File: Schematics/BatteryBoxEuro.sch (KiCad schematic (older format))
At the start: 16 parts, among them K1 JD2912-1Z-12VDC_40A, P1 Conn_WallPlug, U1 Terminal16, U2 F_Distributor, U3 NAC3MPA-1-WOT, U4 DPlusSimulator, U5 Pulser, U6 230V_KfzCharger, X1 X3, X2 12VKfz_Plug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

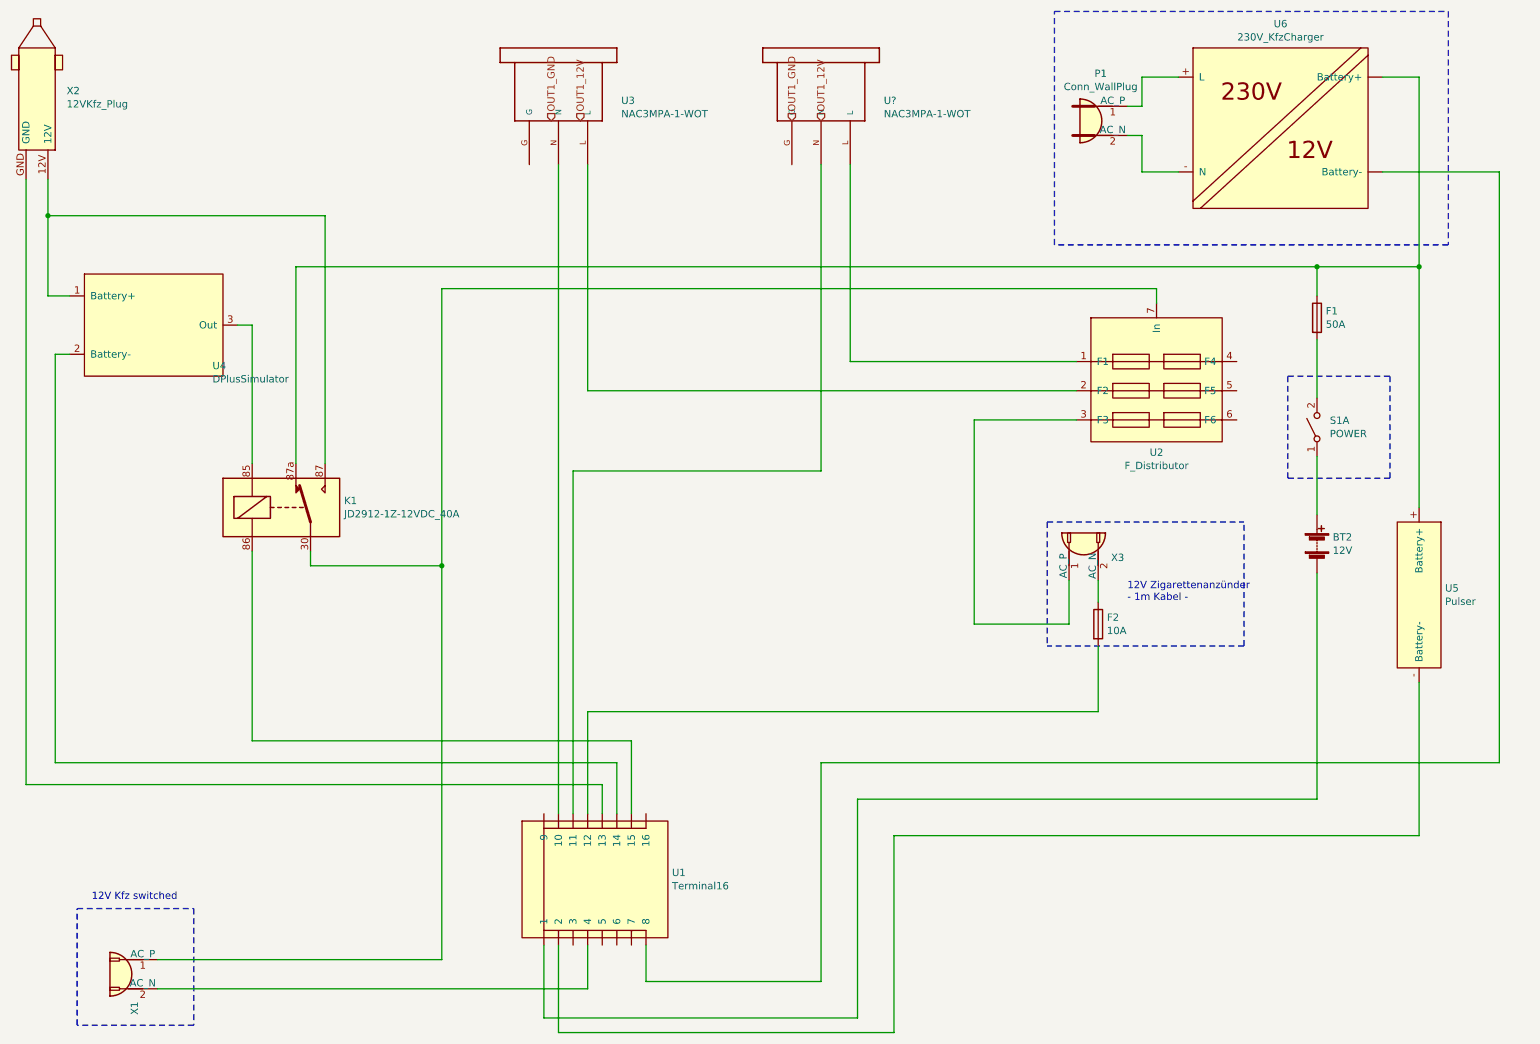
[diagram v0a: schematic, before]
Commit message: rearrange symbols
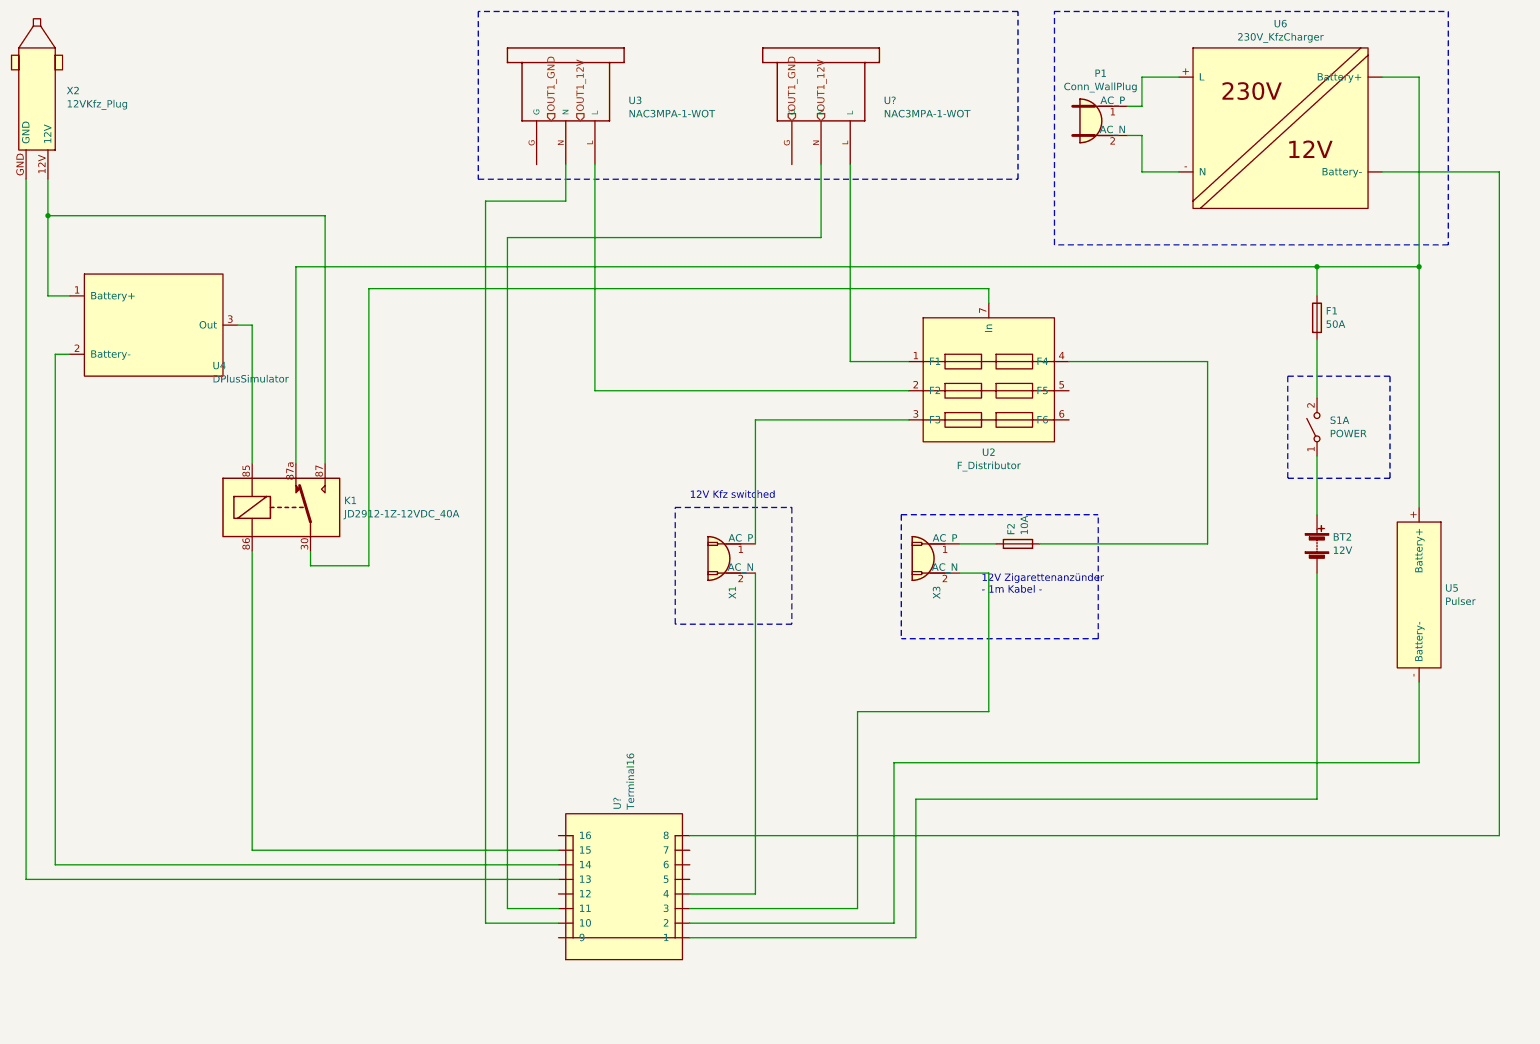
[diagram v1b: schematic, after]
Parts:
- removed U1: Terminal16, symbol MyParts:Terminal16
- added U?: Terminal16, symbol MyParts:Terminal16
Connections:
- net at BT2.2 (-): now also U?.~ (9)
- net at U4.2 (Battery-): now also U?.~ (9)
- net at U5.- (Battery-): now also U?.~ (9)
- net at U2.3 (F3): now also X1.1 (AC_P); no longer X3.1 (AC_P)
- net at U2.4 (F4): now also F2.2
- net at K1.30, K1.31, U2.7 (In): no longer X1.1 (AC_P)
- net at X1.2 (AC_N): now also U?.~ (9)
- net at U6.~ (Battery-): now also U?.~ (9)
- net at K1.86: now also U?.~ (9)
- net at U3.N: now also U?.~ (9)
- net at X2.GND: now also U?.~ (9)
- net at U?.N: now also U?.~ (9)
- net at F2.1: now also X3.1 (AC_P); no longer X3.2 (AC_N)
- new net: U?.~ (9), X3.2 (AC_N)
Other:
- moved on the sheet: F2, U2, U3, X1, X3
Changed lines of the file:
@@
 L MyParts:F_Distributor U2
 U 1 1 5E8A7CC8
-P 8500 2800
-F 0 "U2" H 8500 1977 50  0000 C CNN
-F 1 "F_Distributor" H 8500 1886 50  0000 C CNN
-F 2 "" H 8500 2800 50  0001 C CNN
-F 3 "" H 8500 2800 50  0001 C CNN
-	1    8500 2800
+P 7350 2800
+F 0 "U2" H 7350 1977 50  0000 C CNN
+F 1 "F_Distributor" H 7350 1886 50  0000 C CNN
+F 2 "" H 7350 2800 50  0001 C CNN
+F 3 "" H 7350 2800 50  0001 C CNN
+	1    7350 2800
 	1    0    0    -1
 $EndComp
@@
 Wire Wire Line
 	9600 2850 9600 3250
-$Comp
-L MyParts:Terminal16 U1
-U 1 1 5E8CE450
-P 4750 6550
-F 0 "U1" H 5178 6596 50  0000 L CNN
-F 1 "Terminal16" H 5178 6505 50  0000 L CNN
-F 2 "" H 4800 6600 50  0001 C CNN
-F 3 "" H 4800 6600 50  0001 C CNN
-	1    4750 6550
-	1    0    0    -1
-$EndComp
-Wire Wire Line
-	4300 7000 4300 7500
 $Comp
 L Switch:SW_DPST_x2 S1
@@
 $EndComp
 Wire Wire Line
-	4300 7500 6450 7500
-Wire Wire Line
-	6450 7500 6450 6000
-Wire Wire Line
-	6450 6000 9600 6000
-Wire Wire Line
-	4800 6100 4800 5750
-Wire Wire Line
-	4800 5750 950  5750
-Wire Wire Line
-	4900 6100 4900 5600
-Wire Wire Line
-	4700 6100 4700 5900
-Wire Wire Line
-	4700 5900 750  5900
-Wire Wire Line
-	4400 7000 4400 7600
-Wire Wire Line
-	4400 7600 6700 7600
-Wire Wire Line
-	6700 7600 6700 6250
-Wire Wire Line
-	6700 6250 10300 6250
-Wire Wire Line
-	10300 5200 10300 6250
+	6850 6000 9600 6000
+Wire Wire Line
+	6700 5750 10300 5750
+Wire Wire Line
+	10300 5200 10300 5750
 $Comp
 L Connector:Conn_WallSocket X3
 U 1 1 5EBD0381
-P 8000 4300
-F 0 "X3" V 7956 4112 50  0000 R CNN
-F 1 "X3" V 7911 4112 50  0001 R CNN
-F 2 "" H 7600 4300 50  0001 C CNN
-F 3 "~" H 7600 4300 50  0001 C CNN
-	1    8000 4300
-	0    -1   -1   0
-$EndComp
-Wire Wire Line
-	4600 6100 4600 5400
-Wire Wire Line
-	8100 5400 8100 4950
-Wire Wire Line
-	7900 4500 7900 4800
-Wire Wire Line
-	7900 4800 7250 4800
-Wire Wire Line
-	7250 4800 7250 3400
-Wire Notes Line
-	9100 4950 7750 4950
-Wire Notes Line
-	7750 4100 7750 4950
-Wire Notes Line
-	7750 4100 9100 4100
-Wire Notes Line
-	9100 4950 9100 4100
+P 6950 4350
+F 0 "X3" V 6906 4162 50  0000 R CNN
+F 1 "X3" V 6861 4162 50  0001 R CNN
+F 2 "" H 6550 4350 50  0001 C CNN
+F 3 "~" H 6550 4350 50  0001 C CNN
+	1    6950 4350
+	-1   0    0    -1
+$EndComp
+Wire Notes Line
+	8100 4900 6750 4900
+Wire Notes Line
+	6750 4050 6750 4900
+Wire Notes Line
+	6750 4050 8100 4050
+Wire Notes Line
+	8100 4900 8100 4050
 $Comp
 L Device:Fuse F2
 U 1 1 5EBE1E9A
-P 8100 4800
-F 0 "F2" H 8160 4846 50  0000 L CNN
-F 1 "10A" H 8160 4755 50  0000 L CNN
-F 2 "" V 8030 4800 50  0001 C CNN
-F 3 "~" H 8100 4800 50  0001 C CNN
-	1    8100 4800
-	1    0    0    -1
-$EndComp
-Wire Wire Line
-	8100 4650 8100 4500
+P 7550 4250
+F 0 "F2" H 7610 4296 50  0000 L CNN
+F 1 "10A" H 7610 4205 50  0000 L CNN
+F 2 "" V 7480 4250 50  0001 C CNN
+F 3 "~" H 7550 4250 50  0001 C CNN
+	1    7550 4250
+	0    -1   -1   0
+$EndComp
+Wire Wire Line
+	7350 4450 7150 4450
 Wire Notes Line
 	9400 3100 10100 3100
@@
 Wire Notes Line
 	9400 3800 9400 3100
-Wire Wire Line
-	7250 3400 7950 3400
-Wire Wire Line
-	4600 5400 8100 5400
-Text Notes 8300 4650 0    50   ~ 0
+Text Notes 7300 4600 0    50   ~ 0
 12V Zigarettenanzünder\n- 1m Kabel -
-Wire Wire Line
-	4600 7300 4600 7000
 $Comp
 L MyParts:230V_KfzCharger U6
@@
 Connection ~ 10300 2350
 Wire Wire Line
-	5000 7000 5000 7250
-Wire Wire Line
-	5000 7250 6200 7250
-Wire Wire Line
-	6200 7250 6200 5750
-Wire Wire Line
-	6200 5750 10850 5750
-Wire Wire Line
-	10850 5750 10850 1700
+	10850 6250 10850 1700
 Wire Wire Line
 	10850 1700 10050 1700
@@
 	1    0    0    -1
 $EndComp
-Connection ~ 3600 4400
 Text HLabel 4550 1350 1    50   Input ~ 0
 OUT1_12V
@@
 OUT1_GND
 Wire Wire Line
-	4600 3200 7950 3200
+	4650 3200 6800 3200
 $Comp
 L NAC3MPA-1-WOT:NAC3MPA-1-WOT U3
 U 1 1 5EF1E21B
-P 4200 1450
-F 0 "U3" V 3961 2080 50  0000 L CNN
-F 1 "NAC3MPA-1-WOT" V 4052 2080 50  0000 L CNN
-F 2 "NAC3MPA-1-WOT" H 4200 1450 50  0001 L BNN
-F 3 "" H 4200 1450 50  0001 C CNN
-	1    4200 1450
+P 4250 1450
+F 0 "U3" V 4011 2080 50  0000 L CNN
+F 1 "NAC3MPA-1-WOT" V 4102 2080 50  0000 L CNN
+F 2 "NAC3MPA-1-WOT" H 4250 1450 50  0001 L BNN
+F 3 "" H 4250 1450 50  0001 C CNN
+	1    4250 1450
 	0    1    1    0
 $EndComp
 Wire Wire Line
-	4600 3200 4600 1650
+	4650 3200 4650 1650
 $Comp
 L Connector:Conn_WallPlug P1
@@
 $EndComp
 Wire Wire Line
-	3600 4400 3600 2500
-Wire Wire Line
-	8500 2500 8500 2600
+	3100 4400 3100 2500
+Wire Wire Line
+	7350 2500 7350 2600
 Connection ~ 9600 2350
 Wire Wire Line
@@
 	2700 4300 2700 4400
 Wire Wire Line
-	2700 4400 3600 4400
-Wire Wire Line
-	2300 5600 2300 4300
-Wire Wire Line
-	2300 5600 4900 5600
+	2700 4400 3100 4400
+Wire Wire Line
+	2300 6350 2300 4300
 Wire Wire Line
 	2200 2750 2300 2750
@@
 $EndComp
 Wire Wire Line
-	750  1750 750  5900
+	750  1750 750  6550
 Wire Wire Line
 	900  2000 900  1750
@@
 	900  2550 900  2000
 Wire Wire Line
-	950  2950 950  5750
+	950  2950 950  6450
 Wire Wire Line
 	2300 2750 2300 3700
-Wire Wire Line
-	3600 2500 8500 2500
 $Comp
 L Connector:Conn_WallSocket X1
 U 1 1 5EC190DC
-P 1450 7200
-F 0 "X1" V 1406 7012 50  0000 R CNN
-F 1 "X3" V 1361 7012 50  0001 R CNN
-F 2 "" H 1050 7200 50  0001 C CNN
-F 3 "~" H 1050 7200 50  0001 C CNN
-	1    1450 7200
+P 5550 4350
+F 0 "X1" V 5506 4162 50  0000 R CNN
+F 1 "X3" V 5461 4162 50  0001 R CNN
+F 2 "" H 5150 4350 50  0001 C CNN
+F 3 "~" H 5150 4350 50  0001 C CNN
+	1    5550 4350
 	-1   0    0    -1
 $EndComp
-Text Notes 1200 6700 0    50   ~ 0
+Text Notes 5300 3950 0    50   ~ 0
 12V Kfz switched
 Wire Notes Line
-	1100 7550 1100 6750
-Wire Notes Line
-	1900 7550 1100 7550
-Wire Notes Line
-	1900 6750 1900 7550
-Wire Notes Line
-	1100 6750 1900 6750
-Wire Wire Line
-	1650 7300 4600 7300
-Wire Wire Line
-	1650 7100 3600 7100
-Wire Wire Line
-	3600 4400 3600 7100
-Wire Wire Line
-	6400 3000 7950 3000
-Wire Wire Line
-	4400 1650 4400 6100
+	5200 4800 5200 4000
+Wire Notes Line
+	6000 4800 5200 4800
+Wire Notes Line
+	6000 4000 6000 4800
+Wire Notes Line
+	5200 4000 6000 4000
+Wire Wire Line
+	6400 3000 6800 3000
 $Comp
 L NAC3MPA-1-WOT:NAC3MPA-1-WOT U?
@@
 	0    1    1    0
 $EndComp
-Wire Wire Line
-	4500 6100 4500 3750
-Wire Wire Line
-	4500 3750 6200 3750
 Text HLabel 6000 1350 1    50   Input ~ 0
 OUT1_GND
@@
 OUT1_12V
 Wire Wire Line
-	6200 3750 6200 1650
-Wire Wire Line
 	6400 1650 6400 3000
+$Comp
+L MyParts:Terminal16 U?
+U 1 1 5EF240EF
+P 4850 6500
+F 0 "U?" H 5278 6546 50  0000 L CNN
+F 1 "Terminal16" H 5278 6455 50  0000 L CNN
+F 2 "" H 4900 6550 50  0001 C CNN
+F 3 "" H 4900 6550 50  0001 C CNN
+	1    4850 6500
+	0    -1   -1   0
+$EndComp
+Wire Wire Line
+	4050 6750 4400 6750
+Wire Wire Line
+	5300 6950 6850 6950
+Wire Wire Line
+	6850 6950 6850 6000
+Wire Wire Line
+	5300 6850 6700 6850
+Wire Wire Line
+	6700 6850 6700 5750
+Wire Wire Line
+	5750 4450 5750 6650
+Wire Wire Line
+	4050 6750 4050 2150
+Wire Wire Line
+	4050 2150 6200 2150
+Wire Wire Line
+	6200 2150 6200 1650
+Wire Wire Line
+	4400 6850 3900 6850
+Wire Wire Line
+	3900 6850 3900 1900
+Wire Wire Line
+	3900 1900 4450 1900
+Wire Wire Line
+	4450 1900 4450 1650
+Wire Wire Line
+	750  6550 4400 6550
+Wire Wire Line
+	950  6450 4400 6450
+Wire Wire Line
+	2300 6350 4400 6350
+Wire Wire Line
+	5300 6250 10850 6250
+Wire Wire Line
+	5750 4250 5750 3400
+Wire Wire Line
+	5300 6650 5750 6650
+Wire Wire Line
+	3100 2500 7350 2500
+Wire Wire Line
+	7150 4250 7400 4250
+Wire Wire Line
+	7350 4450 7350 5400
+Wire Notes Line
+	3850 600  3850 1750
+Wire Notes Line
+	3850 1750 7550 1750
+Wire Notes Line
+	7550 1750 7550 600
+Wire Notes Line
+	7550 600  3850 600
+Wire Wire Line
+	5300 6750 6450 6750
+Wire Wire Line
+	6450 6750 6450 5400
+Wire Wire Line
+	6450 5400 7350 5400
+Wire Wire Line
+	5750 3400 6800 3400
+Wire Wire Line
+	7900 3000 8850 3000
+Wire Wire Line
+	8850 3000 8850 4250
+Wire Wire Line
+	8850 4250 7700 4250
 $EndSCHEMATC

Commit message: reduce crossings of wires
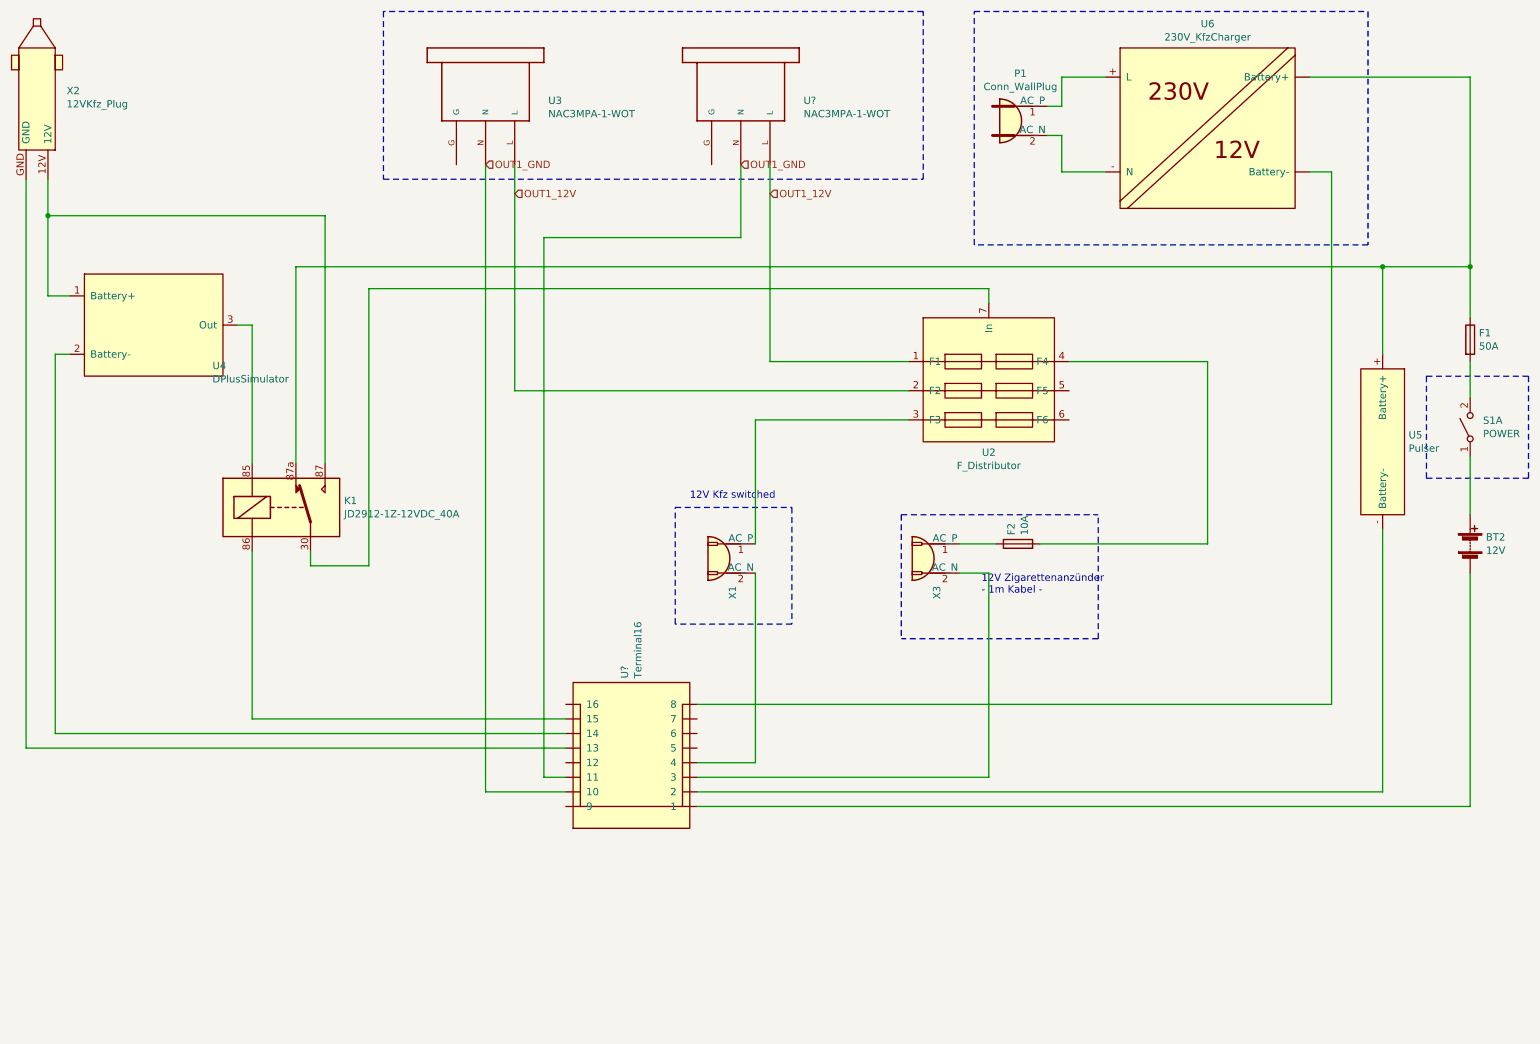
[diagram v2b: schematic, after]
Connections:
- net OUT1_12V: now also U2.1 (F1), U2.2 (F2), U3.L, U?.L
- net OUT1_GND: now also U3.N, U?.N, U?.~ (9)
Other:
- moved on the sheet: BT2, F1, P1, S1A, U3, U5, U6, U?

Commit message: update naming
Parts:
- gave numbers to parts that had none: 2
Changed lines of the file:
@@
 	5850 3000 6800 3000
 $Comp
-L NAC3MPA-1-WOT:NAC3MPA-1-WOT U?
+L NAC3MPA-1-WOT:NAC3MPA-1-WOT U9
 U 1 1 5F024C85
 P 5450 1450
-F 0 "U?" V 5211 2080 50  0000 L CNN
+F 0 "U9" V 5211 2080 50  0000 L CNN
 F 1 "NAC3MPA-1-WOT" V 5302 2080 50  0000 L CNN
 F 2 "NAC3MPA-1-WOT" H 5450 1450 50  0001 L BNN
@@
 	5850 1650 5850 3000
 $Comp
-L MyParts:Terminal16 U?
+L MyParts:Terminal16 U1
 U 1 1 5EF240EF
 P 4900 5600
-F 0 "U?" H 5328 5646 50  0000 L CNN
+F 0 "U1" H 5328 5646 50  0000 L CNN
 F 1 "Terminal16" H 5328 5555 50  0000 L CNN
 F 2 "" H 4950 5650 50  0001 C CNN

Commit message: update readme
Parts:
- U1: footprint (none) -> MyParts:GroundTerminal
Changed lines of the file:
@@
 F 0 "U1" H 5328 5646 50  0000 L CNN
 F 1 "Terminal16" H 5328 5555 50  0000 L CNN
-F 2 "" H 4950 5650 50  0001 C CNN
+F 2 "MyParts:GroundTerminal" H 4950 5650 50  0001 C CNN
 F 3 "" H 4950 5650 50  0001 C CNN
 	1    4900 5600
